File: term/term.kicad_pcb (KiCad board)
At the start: 2 copper layers, 35.6 x 30.5 mm, 39 parts, among them P101 CONN_01X08, P102 XG4C-1631, P103 CONN_01X08, SW101 SW_PUSH

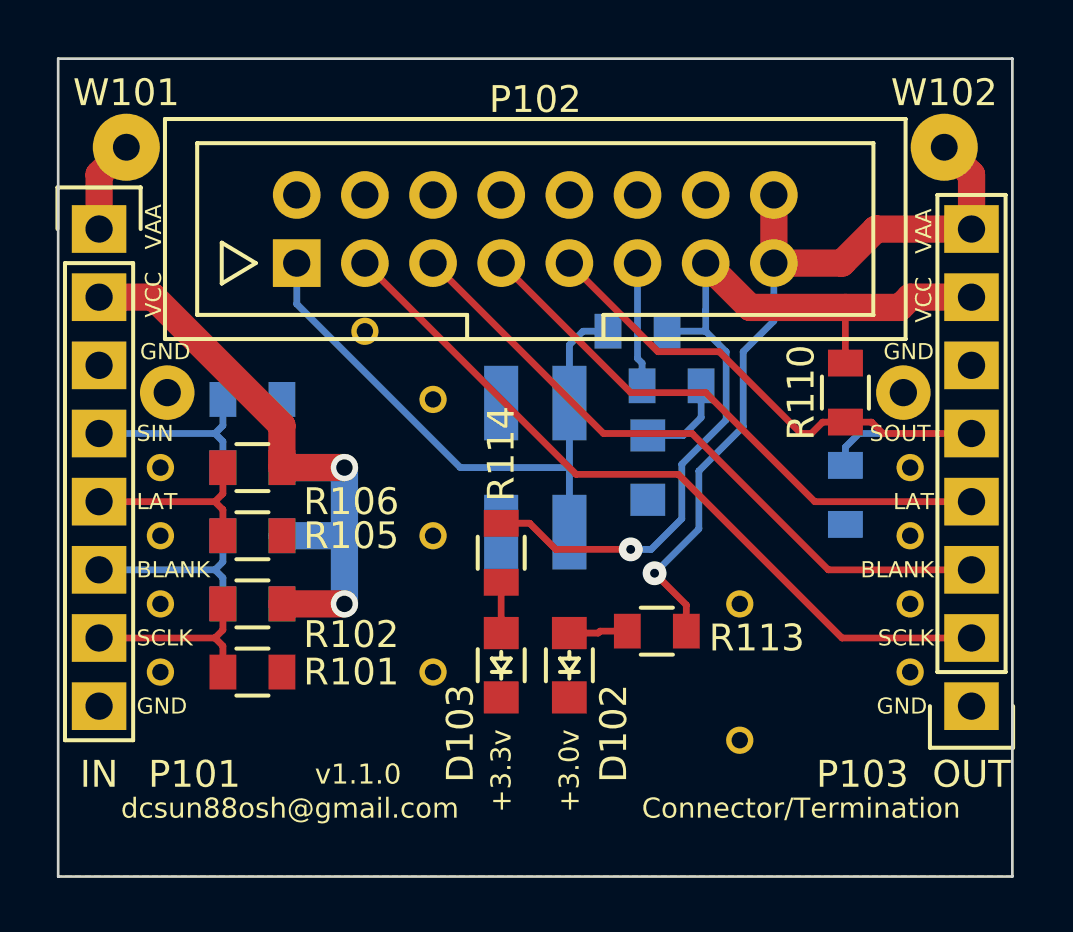
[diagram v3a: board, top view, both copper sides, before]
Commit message: Add DNP to unused resistors on the termination board. Minor clean up of clock board.
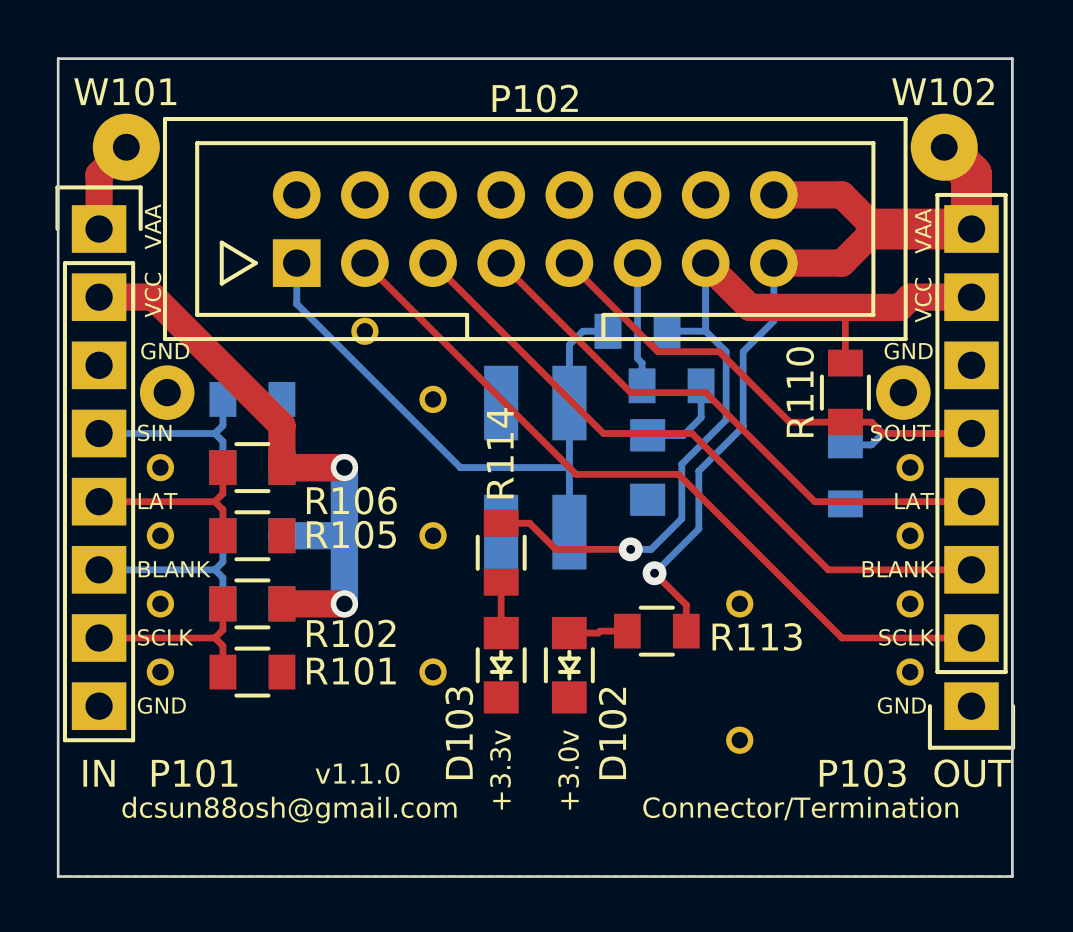
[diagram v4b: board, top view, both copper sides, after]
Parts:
- moved R111 0.76 mm to (156.3, 99.3)
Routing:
- net /VAA_IN: track 29.9 -> 31.7 mm
- net /SOUT: track 23.6 -> 22.5 mm
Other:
- board text added: "RESET"
- board text added: "STATUS"
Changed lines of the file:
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@@
     (area 121.814333 83.769999 167.745667 114.350001)
     (thickness 1.6)
-    (drawings 37)
-    (tracks 111)
+    (drawings 47)
+    (tracks 110)
     (zones 0)
     (modules 39)
@@
     (39 F.Mask user)
     (40 Dwgs.User user)
-    (41 Cmts.User user)
+    (41 Cmts.User user hide)
     (42 Eco1.User user)
     (43 Eco2.User user)
@@
   )
   (module local:R_0805_HandSoldering (layer B.Cu)
-    (at 156.337 100.076 270)
+    (at 156.337 99.314 270)
     (descr "Resistor SMD 0805, hand soldering")
     (tags "resistor 0805")
@@
       (rotate (xyz 0 0 0))
     )
+  )
+  (gr_text STATUS (at 148.971 101.473) (layer B.SilkS)
+    (effects (font (size 0.6 0.6) (thickness 0.15)) (justify right mirror))
+  )
+  (gr_text RESET (at 144.78 104.775) (layer B.SilkS)
+    (effects (font (size 0.6 0.6) (thickness 0.15)) (justify mirror))
+  )
+  (gr_text GND (at 159.512 107.95) (layer B.SilkS)
+    (effects (font (size 0.6 0.6) (thickness 0.15)) (justify left mirror))
+  )
+  (gr_text GND (at 129.921 107.95) (layer B.SilkS)
+    (effects (font (size 0.6 0.6) (thickness 0.15)) (justify right mirror))
+  )
+  (gr_text SIN (at 129.921 97.79) (layer B.SilkS)
+    (effects (font (size 0.6 0.6) (thickness 0.15)) (justify right mirror))
+  )
+  (gr_text VAA (at 129.921 90.17) (layer B.SilkS)
+    (effects (font (size 0.6 0.6) (thickness 0.15)) (justify right mirror))
+  )
+  (gr_text VCC (at 129.921 92.71) (layer B.SilkS)
+    (effects (font (size 0.6 0.6) (thickness 0.15)) (justify right mirror))
+  )
+  (gr_text LAT (at 129.921 100.33) (layer B.SilkS)
+    (effects (font (size 0.6 0.6) (thickness 0.15)) (justify right mirror))
+  )
+  (gr_text BLANK (at 129.921 102.87) (layer B.SilkS)
+    (effects (font (size 0.6 0.6) (thickness 0.15)) (justify right mirror))
+  )
+  (gr_text SCLK (at 129.921 105.41) (layer B.SilkS)
+    (effects (font (size 0.6 0.6) (thickness 0.15)) (justify right mirror))
   )
   (gr_text +3.3v (at 143.51 110.363 90) (layer F.SilkS)
@@
   (segment (start 150.114 99.314) (end 156.21 105.41) (width 0.254) (layer F.Cu) (net 5))
   (segment (start 156.21 105.41) (end 161.036 105.41) (width 0.254) (layer F.Cu) (net 5))
-  (segment (start 156.337 98.298) (end 156.845 97.79) (width 0.254) (layer B.Cu) (net 6))
-  (segment (start 156.845 97.79) (end 161.036 97.79) (width 0.254) (layer B.Cu) (net 6))
-  (segment (start 156.337 98.976) (end 156.337 98.298) (width 0.254) (layer B.Cu) (net 6))
+  (segment (start 156.337 98.214) (end 157.31 98.214) (width 0.254) (layer B.Cu) (net 6))
+  (segment (start 157.734 97.79) (end 161.036 97.79) (width 0.254) (layer B.Cu) (net 6))
+  (segment (start 157.31 98.214) (end 157.734 97.79) (width 0.254) (layer B.Cu) (net 6))
+  (segment (start 156.337 97.366) (end 154.262 97.366) (width 0.254) (layer F.Cu) (net 6))
+  (segment (start 154.262 97.366) (end 151.638 94.742) (width 0.254) (layer F.Cu) (net 6))
+  (segment (start 151.638 94.742) (end 149.352 94.742) (width 0.254) (layer F.Cu) (net 6))
+  (segment (start 149.352 94.742) (end 146.05 91.44) (width 0.254) (layer F.Cu) (net 6))
   (segment (start 157.734 97.79) (end 161.036 97.79) (width 0.254) (layer F.Cu) (net 6))
   (segment (start 156.337 97.366) (end 157.31 97.366) (width 0.254) (layer F.Cu) (net 6))
   (segment (start 157.31 97.366) (end 157.734 97.79) (width 0.254) (layer F.Cu) (net 6))
-  (segment (start 154.686 97.79) (end 155.067 97.79) (width 0.254) (layer F.Cu) (net 6))
-  (segment (start 155.491 97.366) (end 155.067 97.79) (width 0.254) (layer F.Cu) (net 6))
-  (segment (start 156.337 97.366) (end 155.491 97.366) (width 0.254) (layer F.Cu) (net 6))
-  (segment (start 146.05 91.44) (end 149.352 94.742) (width 0.254) (layer F.Cu) (net 6))
-  (segment (start 149.352 94.742) (end 151.638 94.742) (width 0.254) (layer F.Cu) (net 6))
-  (segment (start 151.638 94.742) (end 154.686 97.79) (width 0.254) (layer F.Cu) (net 6))
   (segment (start 133.139 96.52) (end 133.139 97.493) (width 0.254) (layer B.Cu) (net 7))
   (segment (start 133.139 97.493) (end 132.842 97.79) (width 0.254) (layer B.Cu) (net 7))
@@
   (segment (start 158.75 92.71) (end 161.036 92.71) (width 1.016) (layer F.Cu) (net 9))
   (segment (start 158.368999 93.091001) (end 158.75 92.71) (width 1.016) (layer F.Cu) (net 9))
+  (segment (start 153.67 88.9) (end 156.21 88.9) (width 1.016) (layer F.Cu) (net 10))
+  (segment (start 156.21 88.9) (end 157.48 90.17) (width 1.016) (layer F.Cu) (net 10))
   (segment (start 149.225 102.997) (end 150.876 101.346) (width 0.254) (layer B.Cu) (net 10))
   (segment (start 150.876 101.346) (end 150.876 99.187) (width 0.254) (layer B.Cu) (net 10))
@@
   (segment (start 150.409 104.181) (end 150.409 105.156) (width 0.254) (layer F.Cu) (net 10))
   (via (at 149.225 102.997) (size 0.889) (drill 0.3302) (layers F.Cu B.Cu) (net 10))
-  (segment (start 153.67 91.44) (end 153.67 88.9) (width 1.016) (layer F.Cu) (net 10))
-  (segment (start 161.036 90.17) (end 161.036 88.138) (width 1.016) (layer F.Cu) (net 10))
-  (segment (start 161.036 88.138) (end 160.02 87.122) (width 1.016) (layer F.Cu) (net 10))
+  (segment (start 161.036 90.17) (end 161.036 88.138) (width 1.524) (layer F.Cu) (net 10))
+  (segment (start 161.036 88.138) (end 160.02 87.122) (width 1.524) (layer F.Cu) (net 10))
   (segment (start 156.21 91.44) (end 157.48 90.17) (width 1.016) (layer F.Cu) (net 10))
-  (segment (start 157.48 90.17) (end 161.036 90.17) (width 1.016) (layer F.Cu) (net 10))
+  (segment (start 157.48 90.17) (end 161.036 90.17) (width 1.524) (layer F.Cu) (net 10))
   (segment (start 153.67 91.44) (end 156.21 91.44) (width 1.016) (layer F.Cu) (net 10))
   (segment (start 128.524 90.17) (end 128.524 88.138) (width 1.016) (layer F.Cu) (net 11))
